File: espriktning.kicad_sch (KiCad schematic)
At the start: 55 parts, among them J1 USB_C_Receptacle_USB2.0, J2 Conn_Sensor, J3 Conn_Fan, J4 Conn_01x08, Q1 2N7002K, Q2 S8050, Q3 S8050, SW1 Reset, SW2 Flash, U1 ESP-12F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

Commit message: relayout to actually fit
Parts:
- added J6, J7: Conn_01x01_Male, Connector_Pin:Pin_D0.7mm_L6.5mm_W1.8mm_FlatFork, symbol Connector:Conn_01x01_Male
- J4: footprint Connector_PinSocket_1.00mm:PinSocket_1x08_P1.00mm_Vertical -> Connector_PinSocket_1.27mm:PinSocket_1x07_P1.27mm_Vertical; symbol Connector_Generic:Conn_01x08 -> Connector_Generic:Conn_01x07
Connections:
- net +3V3: now also J4.5 (Pin_5); no longer J4.1 (Pin_1)
- net +5V: now also J4.6 (Pin_6); no longer J4.7 (Pin_7)
- net GND: now also J4.7 (Pin_7), J6.1 (Pin_1), J7.1 (Pin_1); no longer J4.8 (Pin_8)
- net GPIO10: no longer J4.6 (Pin_6)
- net GPIO14: now also J4.3 (Pin_3)
- net GPIO9: no longer J4.5 (Pin_5)
- net RX: now also J4.2 (Pin_2); no longer J4.3 (Pin_3)
- net TX: now also J4.1 (Pin_1); no longer J4.2 (Pin_2)

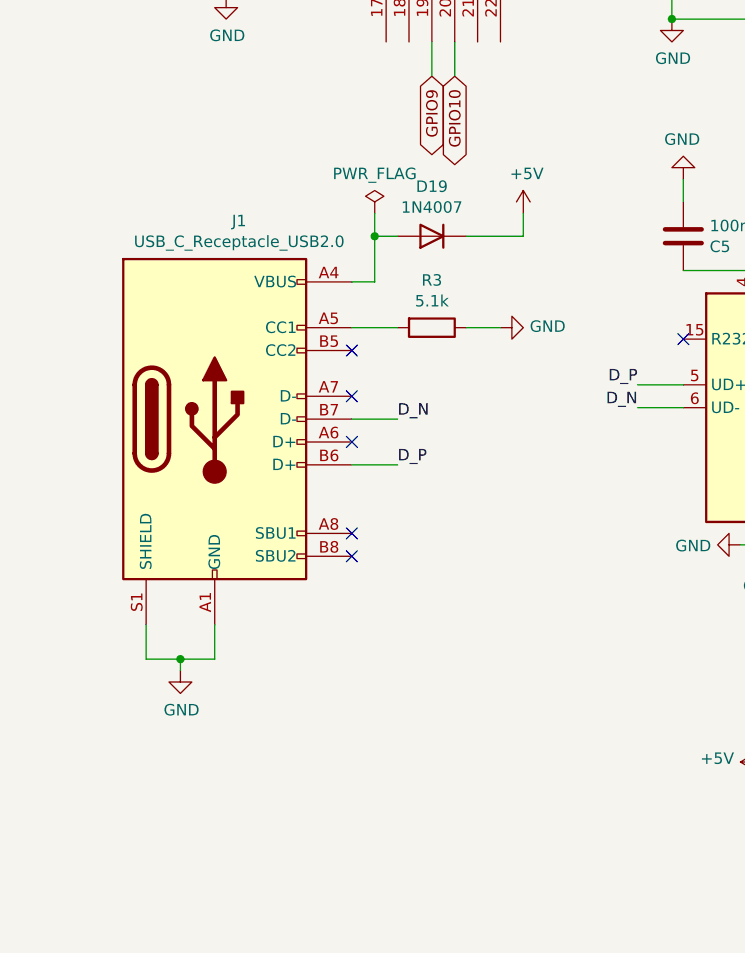
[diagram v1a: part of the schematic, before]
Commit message: fix usb power
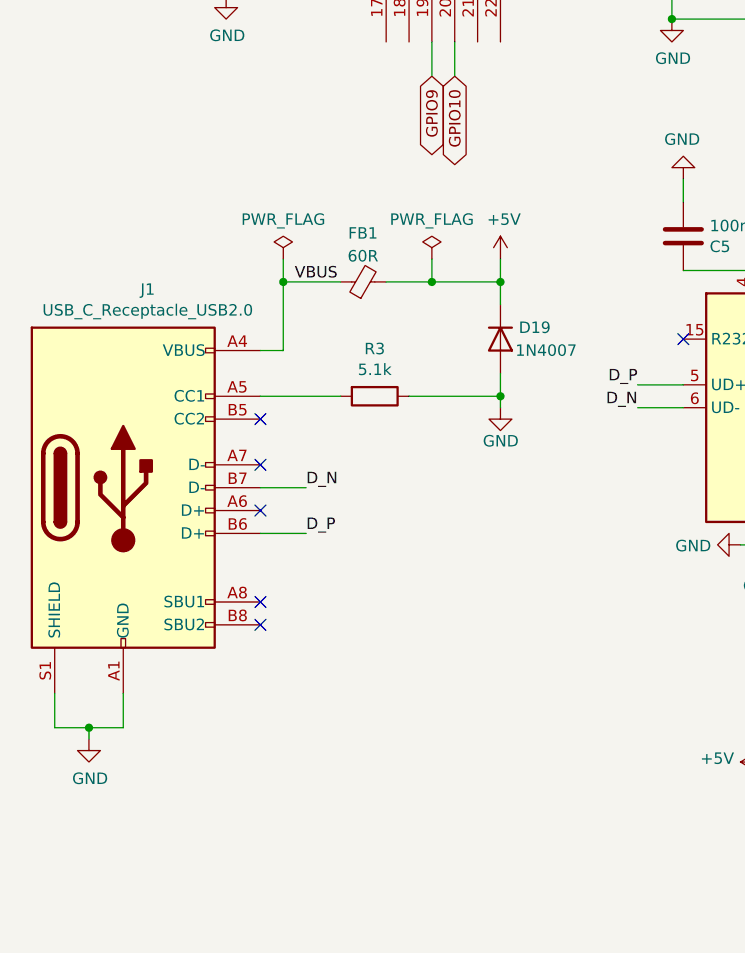
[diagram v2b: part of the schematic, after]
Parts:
- added FB1: 60R, Resistor_SMD:R_0603_1608Metric, symbol Device:FerriteBead_Small
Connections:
- net +5V: now also FB1.2
- net GND: now also D19.2 (A)
- net VBUS: now reaches J1.A4 (VBUS), J1.A9 (VBUS), J1.B4 (VBUS), J1.B9 (VBUS)
- net VBUS: now also FB1.1; no longer D19.2 (A)
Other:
- moved on the sheet: D19, J1, R3

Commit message: support for optional aht10
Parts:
- FB1: value 60R -> 300R
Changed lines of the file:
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@@
     (in_bom yes) (on_board yes) (fields_autoplaced)
     (property "Reference" "FB1" (id 0) (at 54.5719 112.7084 90))
-    (property "Value" "60R" (id 1) (at 54.5719 115.2453 90))
+    (property "Value" "300R" (id 1) (at 54.5719 115.2453 90))
     (property "Footprint" "Resistor_SMD:R_0603_1608Metric" (id 2) (at 54.61 119.888 90)
       (effects (font (size 1.27 1.27)) hide)
@@
     )
     (path "/1ac2416b-7be4-4811-9614-9bf5633972fd"
-      (reference "FB1") (unit 1) (value "60R") (footprint "Resistor_SMD:R_0603_1608Metric")
+      (reference "FB1") (unit 1) (value "300R") (footprint "Resistor_SMD:R_0603_1608Metric")
     )
     (path "/00000000-0000-0000-0000-00006217af1d"
